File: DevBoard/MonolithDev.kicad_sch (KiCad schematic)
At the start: 4 parts

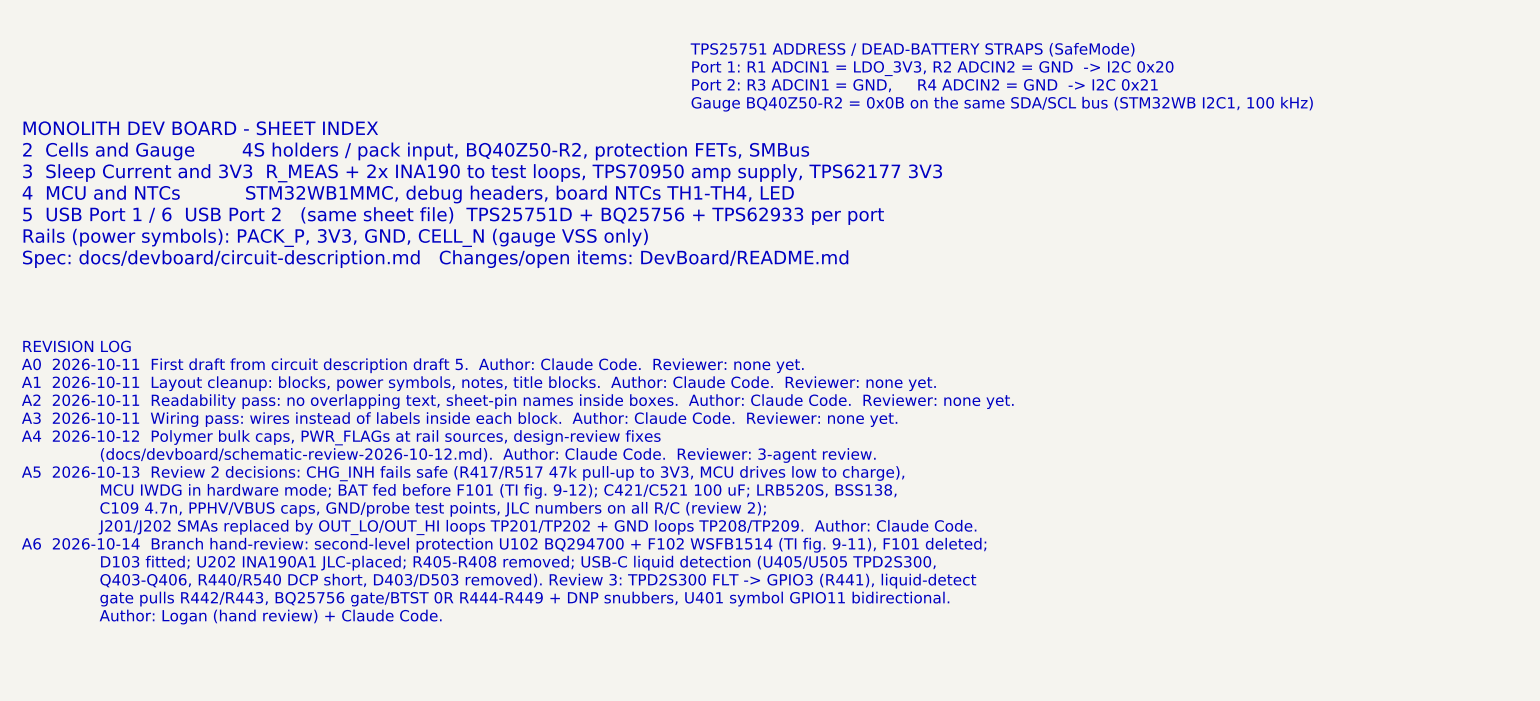
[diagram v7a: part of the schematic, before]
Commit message: Dev board: cost-down pass (about $113 -> $80 per board at 5 boards)
Swaps from docs/devboard/cost-down-2026-10-14.md, datasheet-checked:
- L401/L501 XAL7030 -> SMMS1040-2R2M (Isat 18 A, Irms 12 A, 9 mOhm)
- L402/L502 SRP5030T -> APS0530M3R3H (new footprint L_Coilank_APS0530)
- L201 SRN4018TA -> FNR4030S100MT
- U203 TPS70950 -> HT7550-1, C204/C205 10 uF per Holtek's basic circuit
- C431/C434/C435 47 uF 1210 -> 22 uF 1206 (bank ~114 uF effective)
- JLC basic/preferred equivalents: D103, D401, R410/R412, C105/C206,
  C406, Q103 -> AO3400A
- D301 (out of stock) -> red KT-0603R
- R431/R531 -> bridged solder jumper
- 34 test loops -> bare pads; pin headers hand-soldered
- U301 bought from ST and consigned to JLC

ERC unchanged (0 errors, 8 expected GPIO-to-GND warnings).

Co-Authored-By: Claude Opus 5.5 <noreply@anthropic.com>
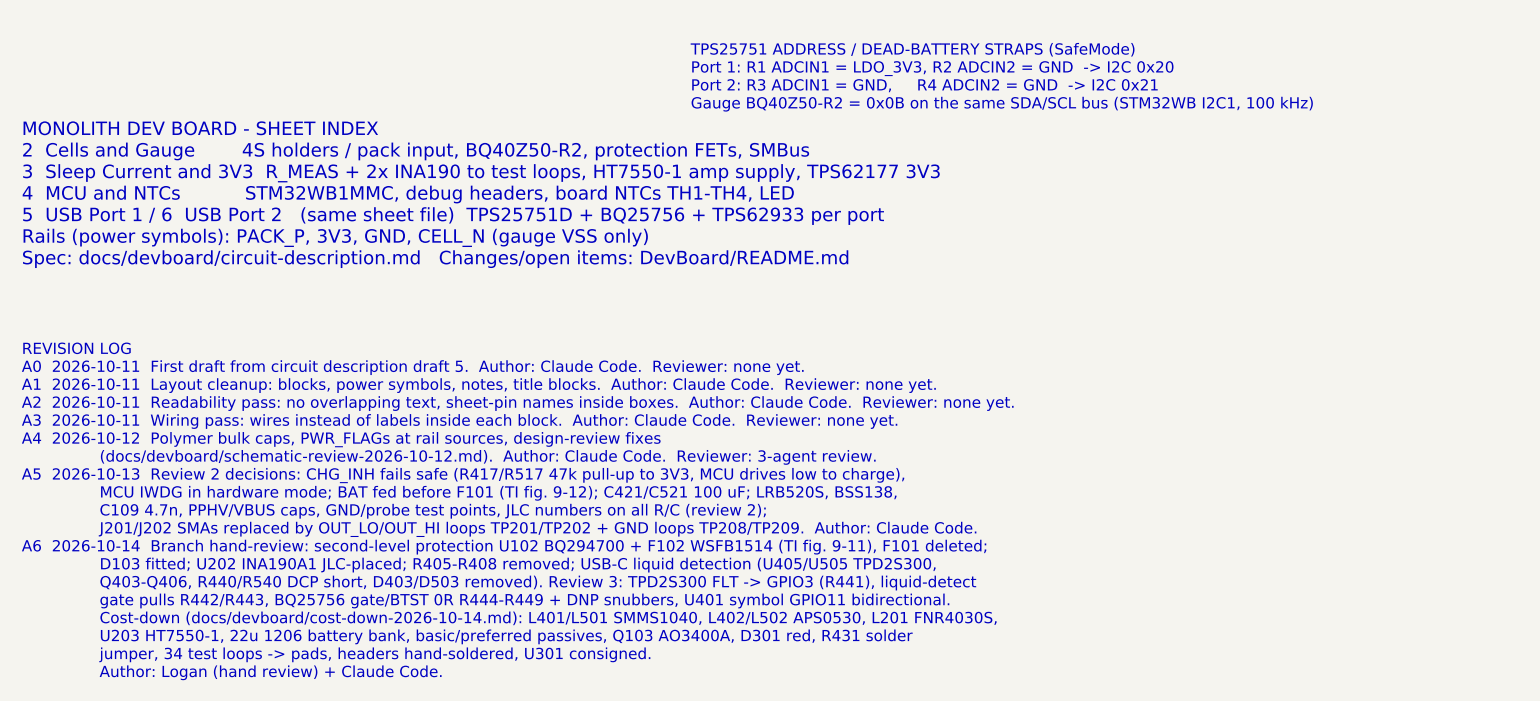
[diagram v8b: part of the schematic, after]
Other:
- note added: "MONOLITH DEV BOARD - SHEET INDEX 2 Cells and Gauge 4S holders / pack input, BQ40Z50-R2, protection FETs, SMBus 3 Sleep Current and 3V3 R_MEAS + 2x INA190 to test loops, HT7550-1 amp supply, TPS62177 3V3 4 MCU and NTCs STM32WB1MMC, debug headers, board NTCs TH1-TH4, LED 5 USB Port 1 / 6 USB Port 2 (same sheet file) TPS25751D + BQ25756 + TPS62933 per port Rails (power symbols): PACK_P, 3V3, GND, CE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"
- note removed: "MONOLITH DEV BOARD - SHEET INDEX 2 Cells and Gauge 4S holders / pack input, BQ40Z50-R2, protection FETs, SMBus 3 Sleep Current and 3V3 R_MEAS + 2x INA190 to test loops, TPS70950 amp supply, TPS62177 3V3 4 MCU and NTCs STM32WB1MMC, debug headers, board NTCs TH1-TH4, LED 5 USB Port 1 / 6 USB Port 2 (same sheet file) TPS25751D + BQ25756 + TPS62933 per port Rails (power symbols): PACK_P, 3V3, GND, CE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"
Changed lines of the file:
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@@
 		(comment 3 "Not reviewed, laid out, built or tested")
 	)
-	(text "MONOLITH DEV BOARD - SHEET INDEX\n2  Cells and Gauge        4S holders / pack input, BQ40Z50-R2, protection FETs, SMBus\n3  Sleep Current and 3V3  R_MEAS + 2x INA190 to test loops, TPS70950 amp supply, TPS62177 3V3\n4  MCU and NTCs           STM32WB1MMC, debug headers, board NTCs TH1-TH4, LED\n5  USB Port 1 / 6  USB Port 2   (same sheet file)  TPS25751D + BQ25756 + TPS62933 per port\nRails (power symbols): PACK_P, 3V3, GND, CELL_N (gauge VSS only)\nSpec: docs/devboard/circuit-description.md   Changes/open items: DevBoard/README.md"
+	(text "MONOLITH DEV BOARD - SHEET INDEX\n2  Cells and Gauge        4S holders / pack input, BQ40Z50-R2, protection FETs, SMBus\n3  Sleep Current and 3V3  R_MEAS + 2x INA190 to test loops, HT7550-1 amp supply, TPS62177 3V3\n4  MCU and NTCs           STM32WB1MMC, debug headers, board NTCs TH1-TH4, LED\n5  USB Port 1 / 6  USB Port 2   (same sheet file)  TPS25751D + BQ25756 + TPS62933 per port\nRails (power symbols): PACK_P, 3V3, GND, CELL_N (gauge VSS only)\nSpec: docs/devboard/circuit-description.md   Changes/open items: DevBoard/README.md"
 		(exclude_from_sim no)
 		(at 30.48 205.74 0)
@@
 		)
 	)
-	(text "REVISION LOG\nA0  2026-10-11  First draft from circuit description draft 5.  Author: Claude Code.  Reviewer: none yet.\nA1  2026-10-11  Layout cleanup: blocks, power symbols, notes, title blocks.  Author: Claude Code.  Reviewer: none yet.\nA2  2026-10-11  Readability pass: no overlapping text, sheet-pin names inside boxes.  Author: Claude Code.  Reviewer: none yet.\nA3  2026-10-11  Wiring pass: wires instead of labels inside each block.  Author: Claude Code.  Reviewer: none yet.\nA4  2026-10-12  Polymer bulk caps, PWR_FLAGs at rail sources, design-review fixes\n                (docs/devboard/schematic-review-2026-10-12.md).  Author: Claude Code.  Reviewer: 3-agent review.\nA5  2026-10-13  Review 2 decisions: CHG_INH fails safe (R417/R517 47k pull-up to 3V3, MCU drives low to charge),\n                MCU IWDG in hardware mode; BAT fed before F101 (TI fig. 9-12); C421/C521 100 uF; LRB520S, BSS138,\n                C109 4.7n, PPHV/VBUS caps, GND/probe test points, JLC numbers on all R/C (review 2);\n                J201/J202 SMAs replaced by OUT_LO/OUT_HI loops TP201/TP202 + GND loops TP208/TP209.  Author: Claude Code.\nA6  2026-10-14  Branch hand-review: second-level protection U102 BQ294700 + F102 WSFB1514 (TI fig. 9-11), F101 deleted;\n                D103 fitted; U202 INA190A1 JLC-placed; R405-R408 removed; USB-C liquid detection (U405/U505 TPD2S300,\n                Q403-Q406, R440/R540 DCP short, D403/D503 removed). Review 3: TPD2S300 FLT -> GPIO3 (R441), liquid-detect\n                gate pulls R442/R443, BQ25756 gate/BTST 0R R444-R449 + DNP snubbers, U401 symbol GPIO11 bidirectional.\n                Author: Logan (hand review) + Claude Code."
+	(text "REVISION LOG\nA0  2026-10-11  First draft from circuit description draft 5.  Author: Claude Code.  Reviewer: none yet.\nA1  2026-10-11  Layout cleanup: blocks, power symbols, notes, title blocks.  Author: Claude Code.  Reviewer: none yet.\nA2  2026-10-11  Readability pass: no overlapping text, sheet-pin names inside boxes.  Author: Claude Code.  Reviewer: none yet.\nA3  2026-10-11  Wiring pass: wires instead of labels inside each block.  Author: Claude Code.  Reviewer: none yet.\nA4  2026-10-12  Polymer bulk caps, PWR_FLAGs at rail sources, design-review fixes\n                (docs/devboard/schematic-review-2026-10-12.md).  Author: Claude Code.  Reviewer: 3-agent review.\nA5  2026-10-13  Review 2 decisions: CHG_INH fails safe (R417/R517 47k pull-up to 3V3, MCU drives low to charge),\n                MCU IWDG in hardware mode; BAT fed before F101 (TI fig. 9-12); C421/C521 100 uF; LRB520S, BSS138,\n                C109 4.7n, PPHV/VBUS caps, GND/probe test points, JLC numbers on all R/C (review 2);\n                J201/J202 SMAs replaced by OUT_LO/OUT_HI loops TP201/TP202 + GND loops TP208/TP209.  Author: Claude Code.\nA6  2026-10-14  Branch hand-review: second-level protection U102 BQ294700 + F102 WSFB1514 (TI fig. 9-11), F101 deleted;\n                D103 fitted; U202 INA190A1 JLC-placed; R405-R408 removed; USB-C liquid detection (U405/U505 TPD2S300,\n                Q403-Q406, R440/R540 DCP short, D403/D503 removed). Review 3: TPD2S300 FLT -> GPIO3 (R441), liquid-detect\n                gate pulls R442/R443, BQ25756 gate/BTST 0R R444-R449 + DNP snubbers, U401 symbol GPIO11 bidirectional.\n                Cost-down (docs/devboard/cost-down-2026-10-14.md): L401/L501 SMMS1040, L402/L502 APS0530, L201 FNR4030S,\n                U203 HT7550-1, 22u 1206 battery bank, basic/preferred passives, Q103 AO3400A, D301 red, R431 solder\n                jumper, 34 test loops -> pads, headers hand-soldered, U301 consigned.\n                Author: Logan (hand review) + Claude Code."
 		(exclude_from_sim no)
-		(at 30.48 246.38 0)
+		(at 30.48 252.73 0)
 		(effects
 			(font
